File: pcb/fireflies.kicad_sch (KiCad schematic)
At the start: 51 parts, among them J1 USB_C_Receptacle_USB2.0_14P, J2 Flash, Q1 AO3416, Q2 AO3416, Q3 AO3416, SW1 SW_Push, SW2 SW_Push, U1 YD3622ARL, U2 CH32V003FxUx, U3 LTR-303ALS-01, U4 XT1861, U5 XC6206PxxxMR

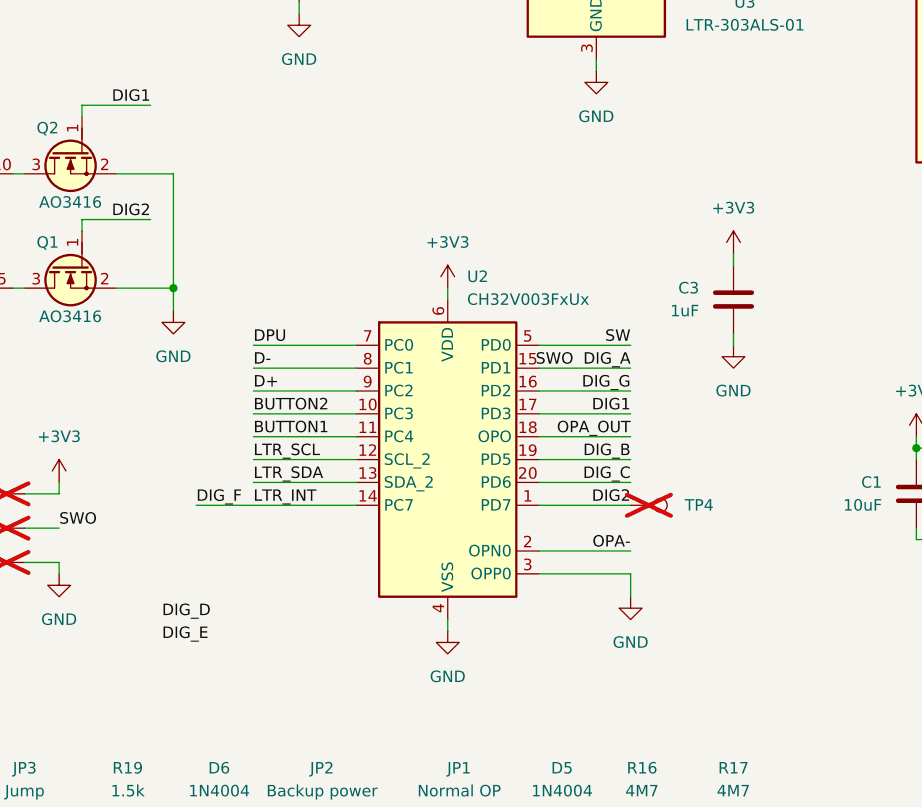
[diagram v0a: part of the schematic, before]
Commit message: Hardware i2c stub
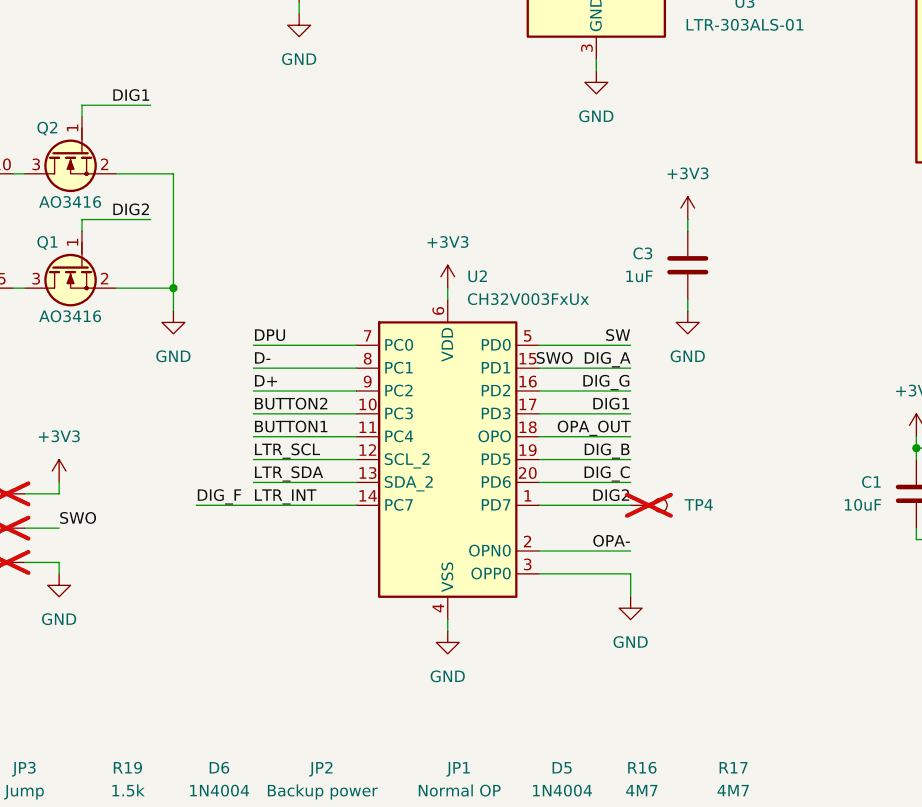
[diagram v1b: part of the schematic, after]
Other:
- moved on the sheet: C3
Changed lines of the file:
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@@
 	(wire
 		(pts
-			(xy 151.13 73.66) (xy 151.13 74.93)
+			(xy 146.05 69.85) (xy 146.05 71.12)
 		)
 		(stroke
@@
 	(wire
 		(pts
-			(xy 151.13 82.55) (xy 151.13 83.82)
+			(xy 146.05 78.74) (xy 146.05 80.01)
 		)
 		(stroke
@@
 		)
 	)
-	(label "DIG_E"
-		(at 87.63 116.84 0)
-		(effects
-			(font
-				(size 1.27 1.27)
-			)
-			(justify left bottom)
-		)
-	)
 	(label "BUTTON1"
 		(at 27.94 97.79 0)
@@
 		)
 	)
-	(label "DIG_D"
-		(at 87.63 114.3 0)
-		(effects
-			(font
-				(size 1.27 1.27)
-			)
-			(justify left bottom)
-		)
-	)
 	(label "DIG_F"
 		(at 91.44 101.6 0)
@@
 	(symbol
 		(lib_id "power:GND")
-		(at 151.13 83.82 0)
+		(at 146.05 80.01 0)
 		(unit 1)
 		(body_style 1)
@@
 		(fields_autoplaced yes)
 		(property "Reference" "#PWR011"
-			(at 151.13 90.17 0)
+			(at 146.05 86.36 0)
 			(hide yes)
 			(show_name no)
@@
 		)
 		(property "Value" "GND"
-			(at 151.13 88.9 0)
+			(at 146.05 85.09 0)
 			(show_name no)
 			(do_not_autoplace no)
@@
 		)
 		(property "Footprint" ""
-			(at 151.13 83.82 0)
+			(at 146.05 80.01 0)
 			(hide yes)
 			(show_name no)
@@
 		)
 		(property "Datasheet" ""
-			(at 151.13 83.82 0)
+			(at 146.05 80.01 0)
 			(hide yes)
 			(show_name no)
@@
 		)
 		(property "Description" "Power symbol creates a global label with name \"GND\" , ground"
-			(at 151.13 83.82 0)
+			(at 146.05 80.01 0)
 			(hide yes)
 			(show_name no)
@@
 	(symbol
 		(lib_id "Device:C")
-		(at 151.13 78.74 0)
+		(at 146.05 74.93 0)
 		(unit 1)
 		(body_style 1)
@@
 		(dnp no)
 		(property "Reference" "C3"
-			(at 147.32 77.4699 0)
+			(at 142.24 73.6599 0)
 			(show_name no)
 			(do_not_autoplace no)
@@
 		)
 		(property "Value" "1uF"
-			(at 147.32 80.0099 0)
+			(at 142.24 76.1999 0)
 			(show_name no)
 			(do_not_autoplace no)
@@
 		)
 		(property "Footprint" "Capacitor_SMD:C_0402_1005Metric"
-			(at 152.0952 82.55 0)
+			(at 147.0152 78.74 0)
 			(hide yes)
 			(show_name no)
@@
 		)
 		(property "Datasheet" ""
-			(at 151.13 78.74 0)
+			(at 146.05 74.93 0)
 			(hide yes)
 			(show_name no)
@@
 		)
 		(property "Description" "Unpolarized capacitor"
-			(at 151.13 78.74 0)
+			(at 146.05 74.93 0)
 			(hide yes)
 			(show_name no)
@@
 		)
 		(property "LCSC Part #" "C52923"
-			(at 151.13 78.74 0)
+			(at 146.05 74.93 0)
 			(hide yes)
 			(show_name no)
@@
 	(symbol
 		(lib_id "power:+3V3")
-		(at 151.13 73.66 0)
+		(at 146.05 69.85 0)
 		(unit 1)
 		(body_style 1)
@@
 		(fields_autoplaced yes)
 		(property "Reference" "#PWR010"
-			(at 151.13 77.47 0)
+			(at 146.05 73.66 0)
 			(hide yes)
 			(show_name no)
@@
 		)
 		(property "Value" "+3V3"
-			(at 151.13 68.58 0)
+			(at 146.05 64.77 0)
 			(show_name no)
 			(do_not_autoplace no)
@@
 		)
 		(property "Footprint" ""
-			(at 151.13 73.66 0)
+			(at 146.05 69.85 0)
 			(hide yes)
 			(show_name no)
@@
 		)
 		(property "Datasheet" ""
-			(at 151.13 73.66 0)
+			(at 146.05 69.85 0)
 			(hide yes)
 			(show_name no)
@@
 		)
 		(property "Description" "Power symbol creates a global label with name \"+3V3\""
-			(at 151.13 73.66 0)
+			(at 146.05 69.85 0)
 			(hide yes)
 			(show_name no)
